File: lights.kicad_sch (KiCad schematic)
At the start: 27 parts, among them Q1 2N7002, Q2 2N7002, U1 EL3H7

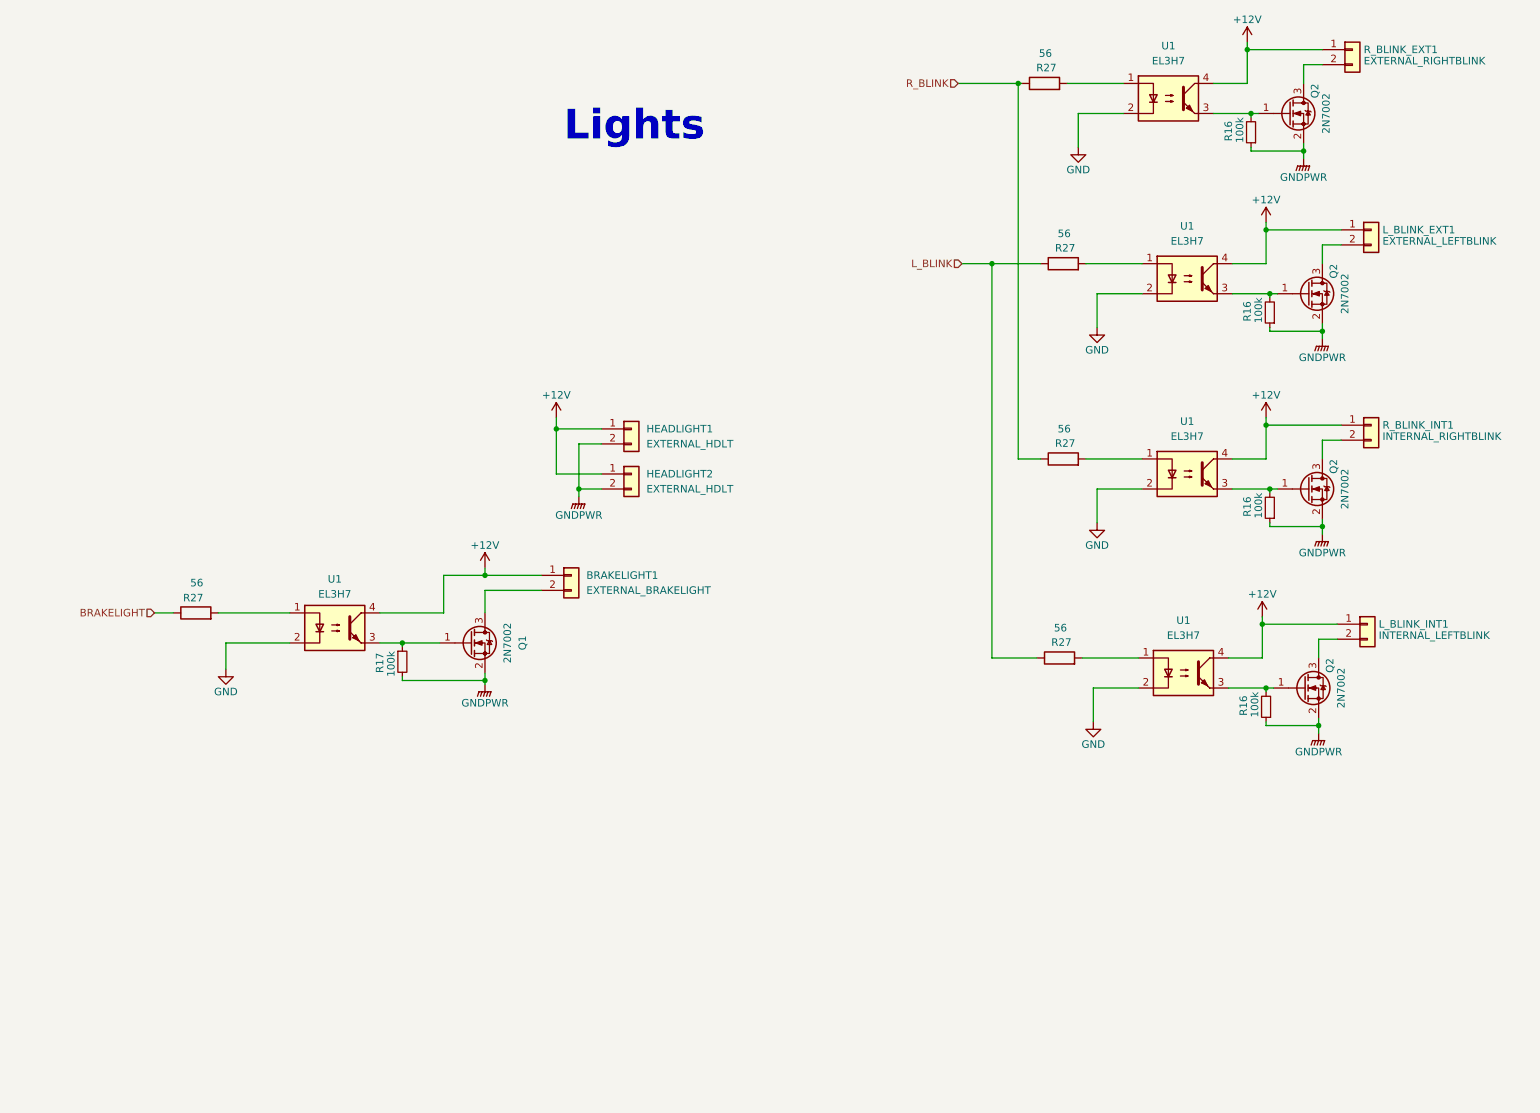
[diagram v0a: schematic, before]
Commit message: Fixed leaderSOM connections, removed optocouplers for lighting and fans, found new MOSFETs
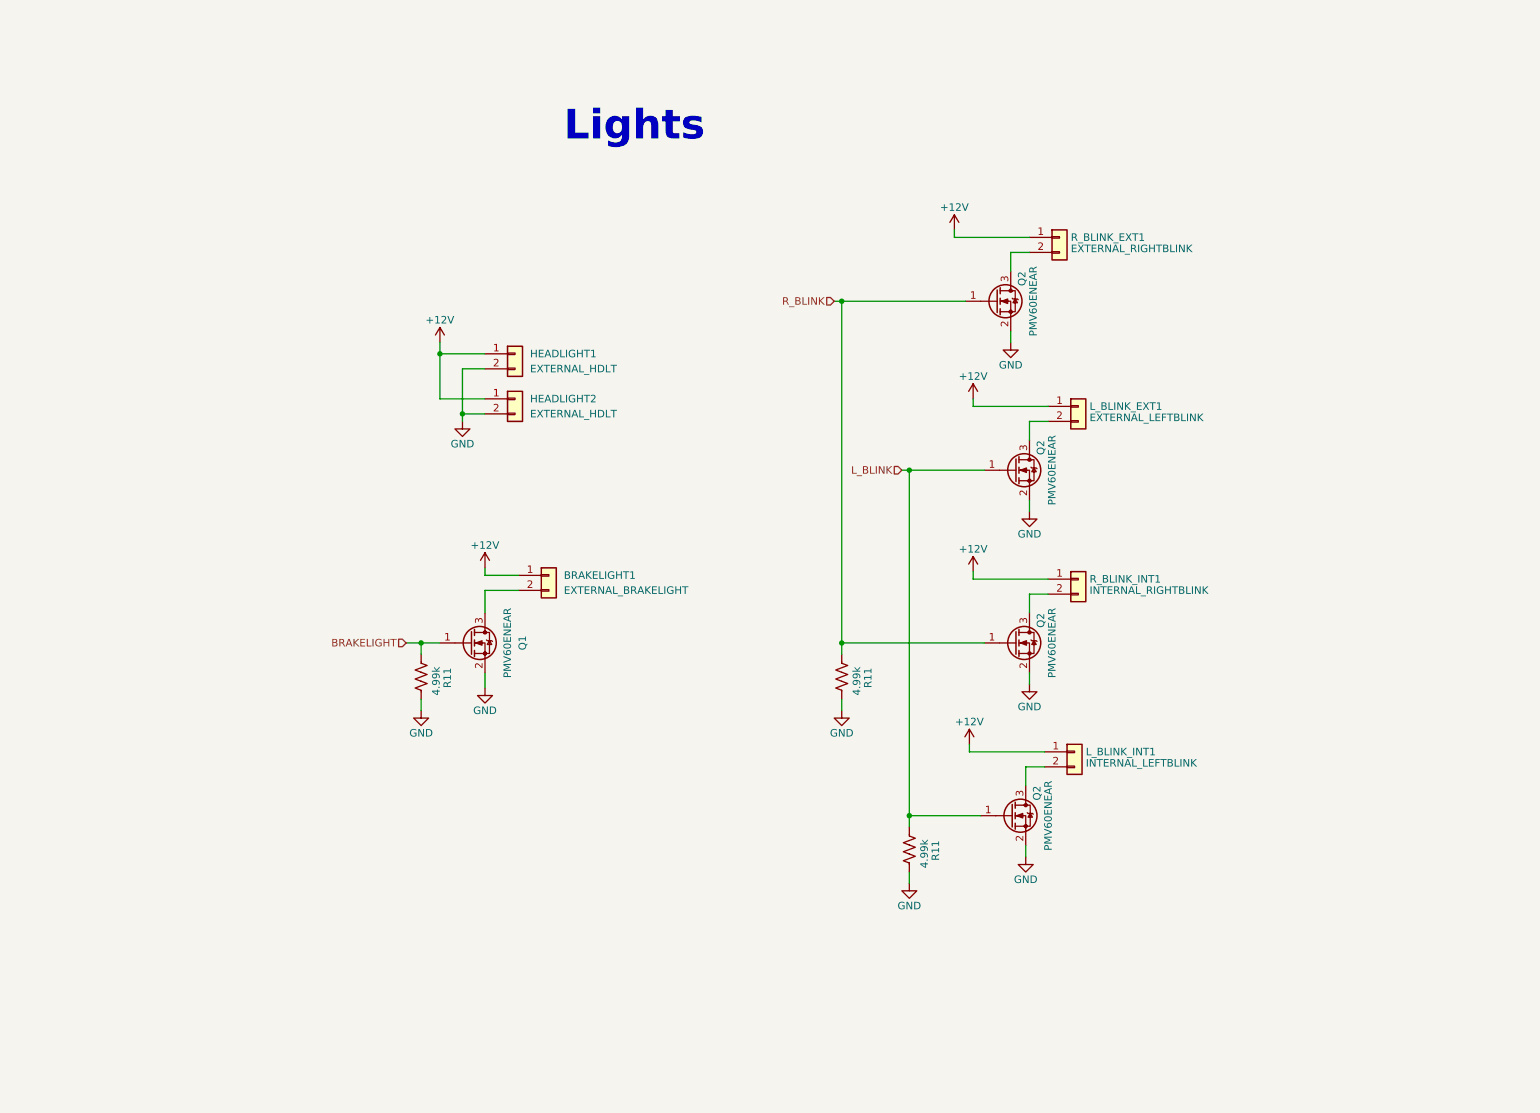
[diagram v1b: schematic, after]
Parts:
- removed R16 (x4), R17: 100k, Resistor_SMD:R_0805_2012Metric, symbol Device:R_Small
- removed R27 (x5): 56, Resistor_SMD:R_0805_2012Metric, symbol Device:R
- removed U1 (x5): EL3H7, Package_SO:SOP-4_4.4x2.6mm_P1.27mm, symbol Isolator:EL817
- added R11 (x3): 4.99k, Resistor_SMD:R_0805_2012Metric, symbol Device:R_US
- Q1, Q2: value 2N7002 -> PMV60ENEAR; Mouser PN 771-2N7002HR -> 771-PMV60ENEAR; PN 2N7002HR -> PMV60ENEAR
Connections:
- net GNDPWR is gone; now on net GND: HEADLIGHT1.2 (Pin_2), HEADLIGHT2.2 (Pin_2), Q1.2 (S), Q2.2 (S), Q2.2 (S), Q2.2 (S), Q2.2 (S)
- net BRAKELIGHT: now also Q1.1 (G), R11.1
- net GND: now also R11.2, R11.2, R11.2
- net L_BLINK: now also Q2.1 (G), Q2.1 (G), R11.1
- net R_BLINK: now also Q2.1 (G), Q2.1 (G), R11.1
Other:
- moved on the sheet: BRAKELIGHT1, HEADLIGHT1, HEADLIGHT2, L_BLINK_EXT1, L_BLINK_INT1, Q2, R_BLINK_EXT1, R_BLINK_INT1

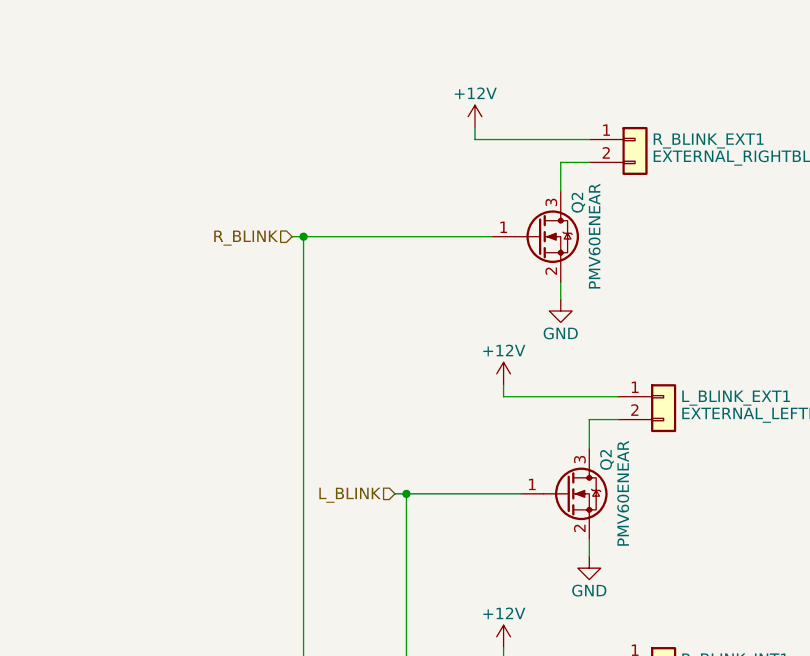
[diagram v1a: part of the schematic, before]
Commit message: Added I2C GPIO expander to reduce GPIO pins from LeaderSOM and replace 555 timer circuit. Adjusted ignition switch signals.
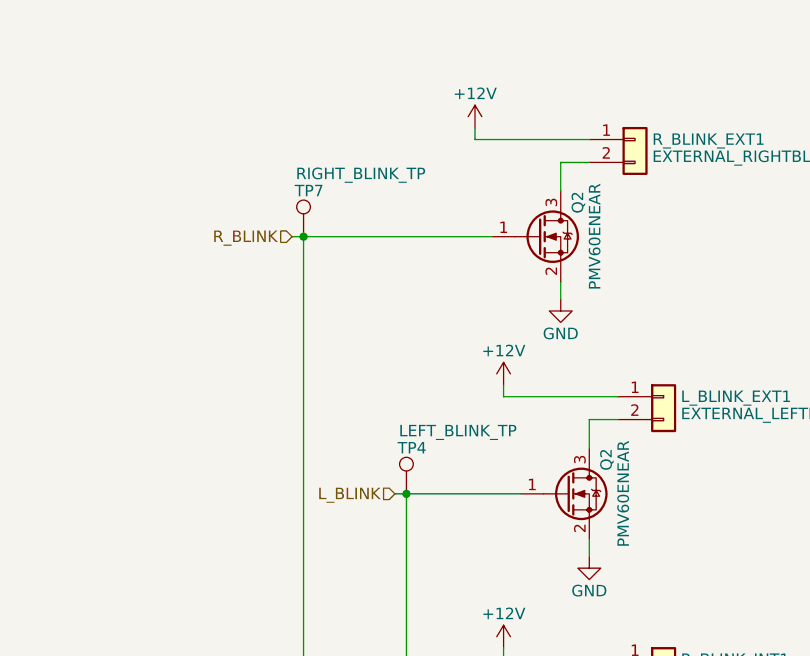
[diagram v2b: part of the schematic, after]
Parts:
- added TP4: LEFT_BLINK_TP, TestPoint:TestPoint_Pad_1.5x1.5mm, symbol Connector:TestPoint
- added TP7: RIGHT_BLINK_TP, TestPoint:TestPoint_Pad_1.5x1.5mm, symbol Connector:TestPoint
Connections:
- net L_BLINK: now also TP4.1
- net R_BLINK: now also TP7.1
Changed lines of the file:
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@@
+    )
+  )
+  (symbol (lib_id "Connector:TestPoint") (at 152.4 62.865 0) (unit 1)
+    (in_bom yes) (on_board yes) (dnp no)
+    (property "Reference" "TP7" (at 153.035 57.785 0)
+      (effects (font (size 1.27 1.27)))
+    )
+    (property "Value" "RIGHT_BLINK_TP" (at 158.75 55.88 0)
+      (effects (font (size 1.27 1.27)))
+    )
+    (property "Footprint" "TestPoint:TestPoint_Pad_1.5x1.5mm" (at 157.48 62.865 0)
+      (effects (font (size 1.27 1.27)) hide)
+    )
+    (property "Datasheet" "~" (at 157.48 62.865 0)
+      (effects (font (size 1.27 1.27)) hide)
+    )
+    (pin "1")
+    (instances
+      (project "Controls-LightingPCB"
+        (path "/229b82f0-5048-47d6-8bc8-0bcee42eb4bc"
+          (reference "TP7") (unit 1)
+        )
+      )
+      (project "Controls-LeaderDaughterPCB"
+        (path "/c7871779-04fe-4705-8150-20a4dd0ef44f"
+          (reference "TP6") (unit 1)
+        )
+        (path "/c7871779-04fe-4705-8150-20a4dd0ef44f/f7827f80-0f50-4e4f-b2cd-ff48878538ae"
+          (reference "TP4") (unit 1)
+        )
+      )
     )
   )
@@
         )
       )
+    )
+  )
+  (symbol (lib_id "Connector:TestPoint") (at 163.83 91.44 0) (unit 1)
+    (in_bom yes) (on_board yes) (dnp no)
+    (property "Reference" "TP4" (at 164.465 86.36 0)
+      (effects (font (size 1.27 1.27)))
+    )
+    (property "Value" "LEFT_BLINK_TP" (at 169.545 84.455 0)
+      (effects (font (size 1.27 1.27)))
+    )
+    (property "Footprint" "TestPoint:TestPoint_Pad_1.5x1.5mm" (at 168.91 91.44 0)
+      (effects (font (size 1.27 1.27)) hide)
+    )
+    (property "Datasheet" "~" (at 168.91 91.44 0)
+      (effects (font (size 1.27 1.27)) hide)
+    )
+    (pin "1")
+    (instances
+      (project "Controls-LightingPCB"
+        (path "/229b82f0-5048-47d6-8bc8-0bcee42eb4bc"
+          (reference "TP4") (unit 1)
+        )
+      )
+      (project "Controls-LeaderDaughterPCB"
+        (path "/c7871779-04fe-4705-8150-20a4dd0ef44f"
+          (reference "TP7") (unit 1)
+        )
+        (path "/c7871779-04fe-4705-8150-20a4dd0ef44f/f7827f80-0f50-4e4f-b2cd-ff48878538ae"
+          (reference "TP5") (unit 1)
+        )
+      )

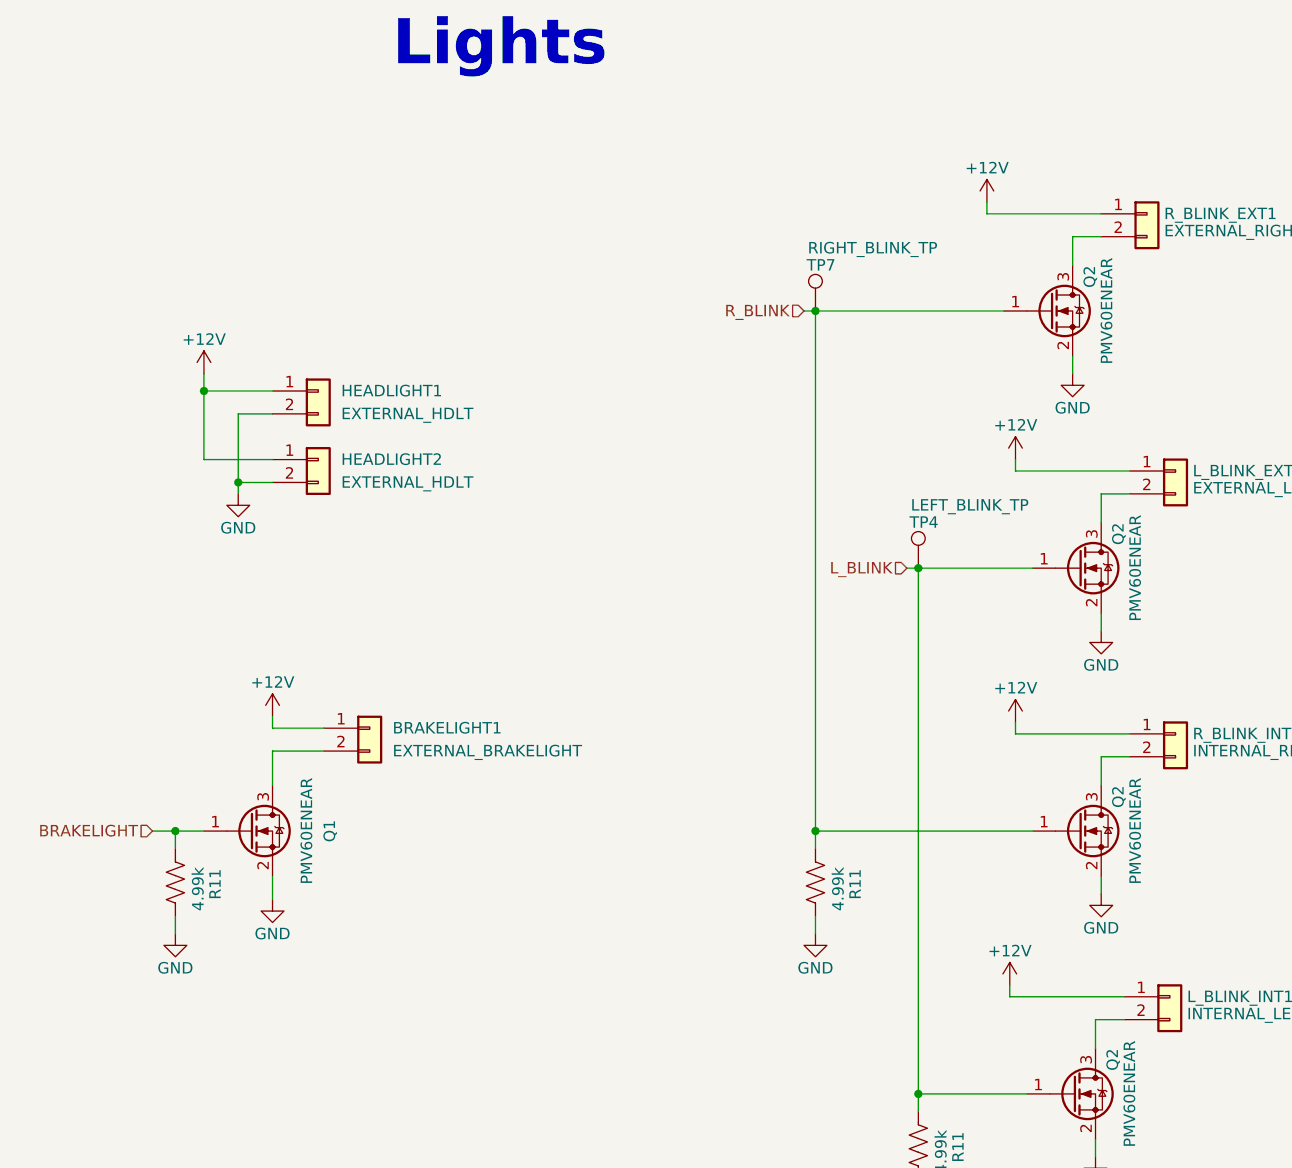
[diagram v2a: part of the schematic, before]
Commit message: Added debouncing, bypass caps, pull up and down resistors, and current limiting resistors. Removed some TPs.
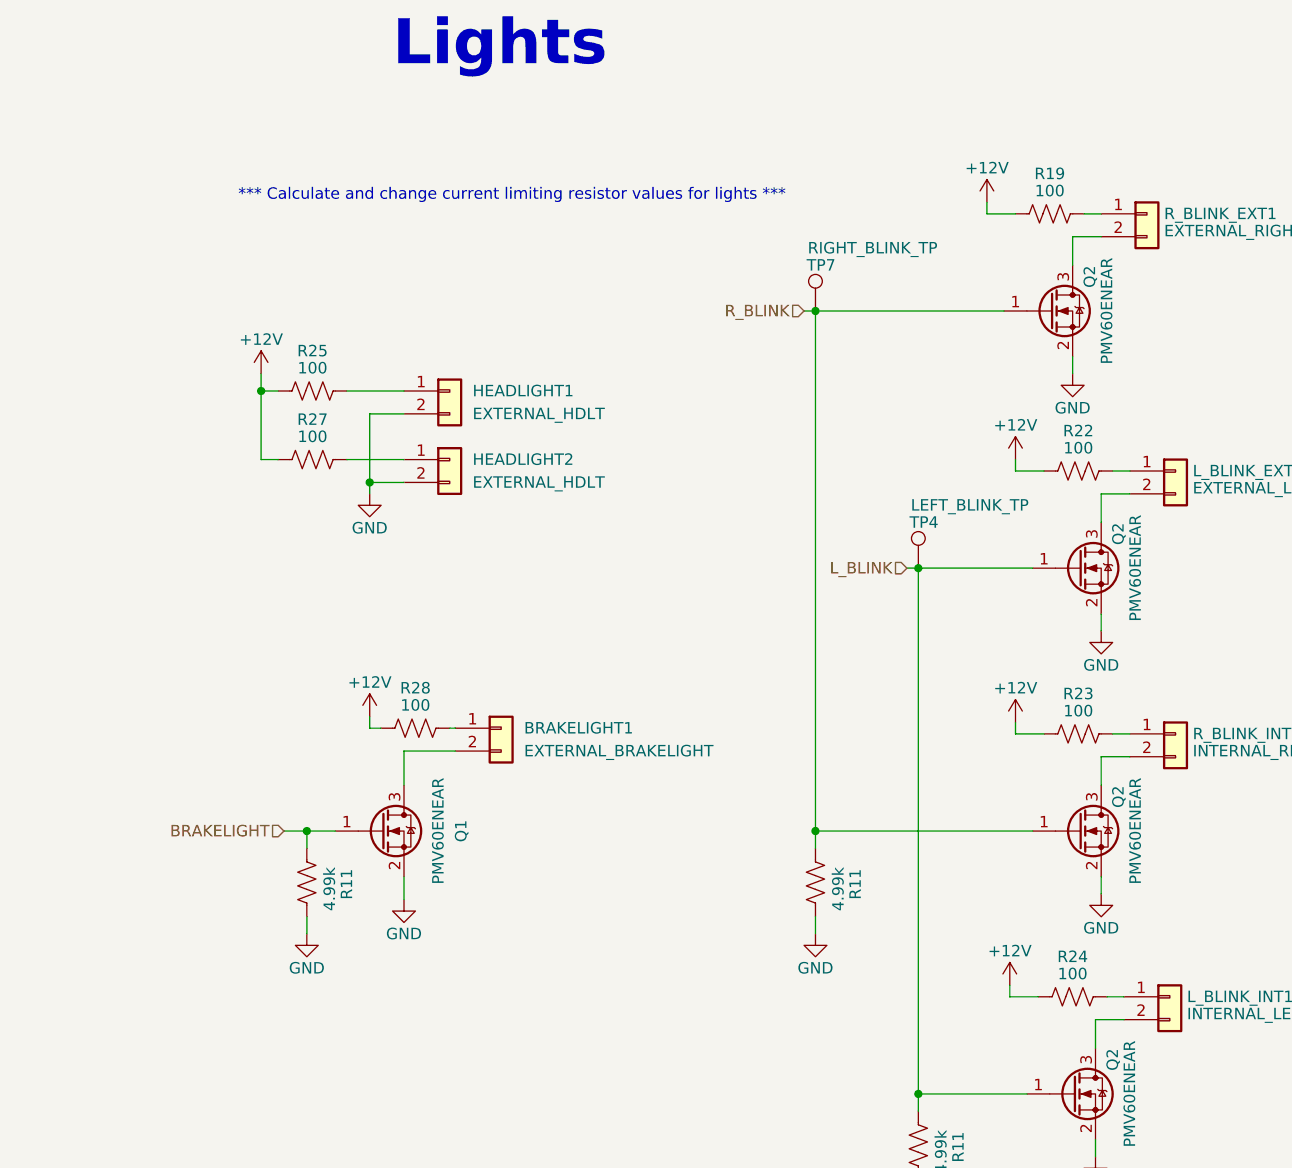
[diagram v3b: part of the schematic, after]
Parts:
- added R19, R22, R23, R24, R25, R27, R28: 100, symbol Device:R_US
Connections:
- net +12V: now also R19.1, R22.1, R23.1, R24.1, R25.1, R27.1, R28.1; no longer BRAKELIGHT1.1 (Pin_1), HEADLIGHT1.1 (Pin_1), HEADLIGHT2.1 (Pin_1), L_BLINK_EXT1.1 (Pin_1), L_BLINK_INT1.1 (Pin_1), R_BLINK_EXT1.1 (Pin_1), R_BLINK_INT1.1 (Pin_1)
- new net: HEADLIGHT1.1 (Pin_1), R25.2
- new net: L_BLINK_INT1.1 (Pin_1), R24.2
- new net: BRAKELIGHT1.1 (Pin_1), R28.2
- new net: R23.2, R_BLINK_INT1.1 (Pin_1)
- new net: R19.2, R_BLINK_EXT1.1 (Pin_1)
- new net: L_BLINK_EXT1.1 (Pin_1), R22.2
- new net: HEADLIGHT2.1 (Pin_1), R27.2
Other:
- note added: "*** Calculate and change current limiting resistor values for lights ***"
- moved on the sheet: BRAKELIGHT1, HEADLIGHT1, HEADLIGHT2, Q1, R11

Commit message: assigned footprints
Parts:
- R19, R22, R23, R24, R25, R27, R28: footprint (none) -> Resistor_SMD:R_0805_2012Metric
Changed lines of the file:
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@@
       (effects (font (size 1.27 1.27)))
     )
-    (property "Footprint" "" (at 96.774 70.739 90)
+    (property "Footprint" "Resistor_SMD:R_0805_2012Metric" (at 96.774 70.739 90)
       (effects (font (size 1.27 1.27)) hide)
     )
@@
       (effects (font (size 1.27 1.27)))
     )
-    (property "Footprint" "" (at 181.229 138.049 90)
+    (property "Footprint" "Resistor_SMD:R_0805_2012Metric" (at 181.229 138.049 90)
       (effects (font (size 1.27 1.27)) hide)
     )
@@
       (effects (font (size 1.27 1.27)))
     )
-    (property "Footprint" "" (at 108.204 108.204 90)
+    (property "Footprint" "Resistor_SMD:R_0805_2012Metric" (at 108.204 108.204 90)
       (effects (font (size 1.27 1.27)) hide)
     )
@@
       (effects (font (size 1.27 1.27)))
     )
-    (property "Footprint" "" (at 181.864 79.629 90)
+    (property "Footprint" "Resistor_SMD:R_0805_2012Metric" (at 181.864 79.629 90)
       (effects (font (size 1.27 1.27)) hide)
     )
@@
       (effects (font (size 1.27 1.27)))
     )
-    (property "Footprint" "" (at 96.774 78.359 90)
+    (property "Footprint" "Resistor_SMD:R_0805_2012Metric" (at 96.774 78.359 90)
       (effects (font (size 1.27 1.27)) hide)
     )
@@
       (effects (font (size 1.27 1.27)))
     )
-    (property "Footprint" "" (at 181.864 108.839 90)
+    (property "Footprint" "Resistor_SMD:R_0805_2012Metric" (at 181.864 108.839 90)
       (effects (font (size 1.27 1.27)) hide)
     )
@@
       (effects (font (size 1.27 1.27)))
     )
-    (property "Footprint" "" (at 178.689 51.054 90)
-      (effects (font (size 1.27 1.27)) hide)
-    )
+    (property "Footprint" "Resistor_SMD:R_0805_2012Metric" (at 178.689 51.054 90)
+      (effects (font (size 1.27 1.27)) hide)
+    )
